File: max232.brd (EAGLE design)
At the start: 60 x 50 mm, 82 parts, among them U1 MAX3232CDE4, U2 MAX3232CDE4

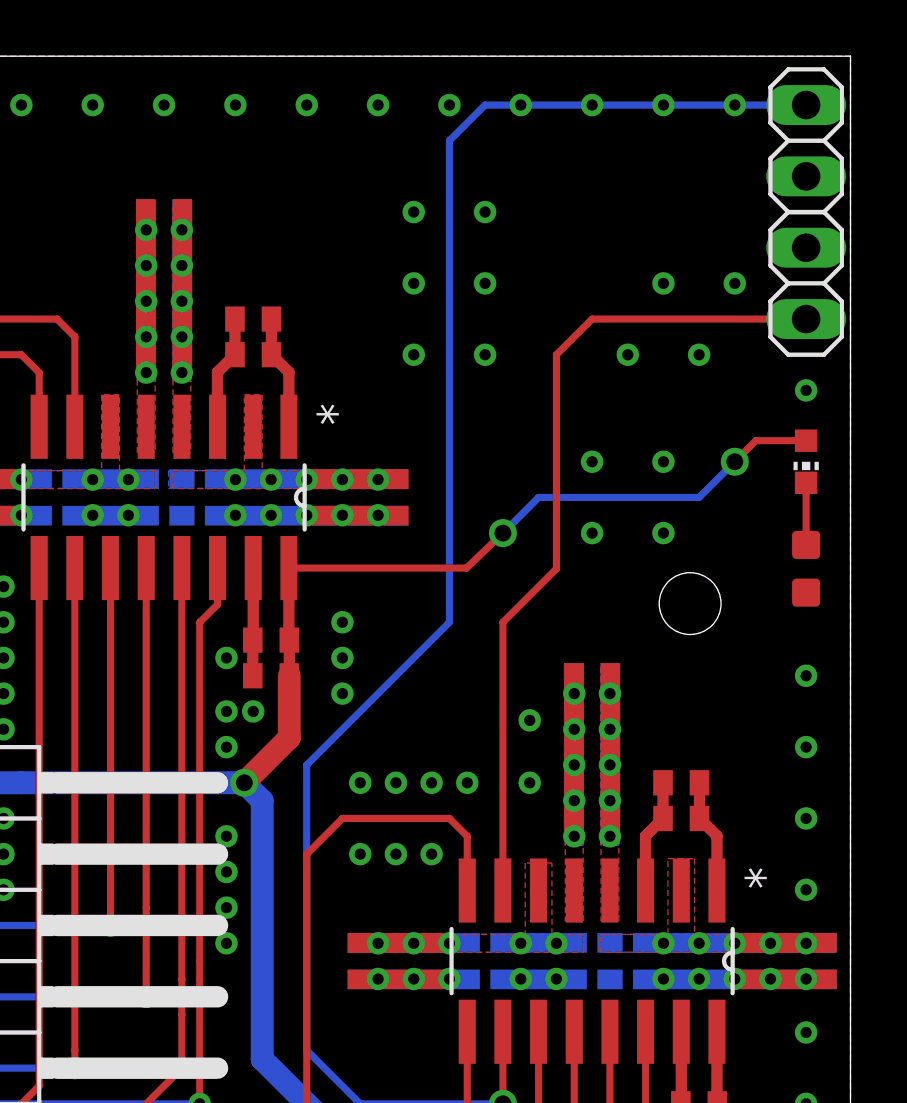
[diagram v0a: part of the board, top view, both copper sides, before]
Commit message: fixed DRC in max232
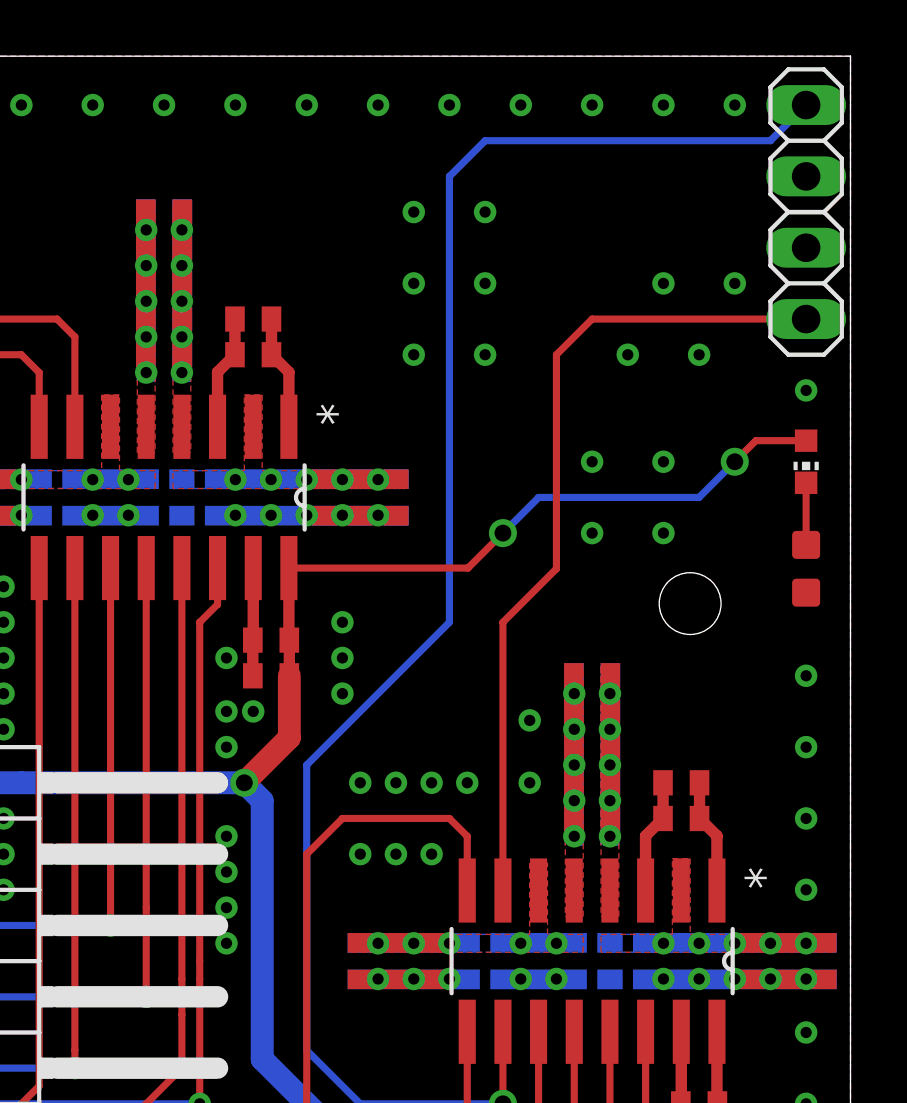
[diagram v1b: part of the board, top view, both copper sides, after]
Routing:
- net TIN: track 58.1 -> 57.3 mm
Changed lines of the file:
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@@
 <setting verticaltext="up"/>
 </settings>
-<grid distance="0.05" unitdist="inch" unit="mm" style="lines" multiple="1" display="no" altdistance="12.5" altunitdist="mil" altunit="mm"/>
+<grid distance="0.05" unitdist="inch" unit="mm" style="lines" multiple="1" display="no" altdistance="6.25" altunitdist="mil" altunit="mil"/>
 <layers>
 <layer number="1" name="Top" color="4" fill="1" visible="yes" active="yes"/>
@@
 <wire x1="55.245" y1="11.415" x2="55.26" y2="11.43" width="0.8128" layer="1"/>
 <wire x1="40.02" y1="25.7325" x2="38.4175" y2="24.13" width="0.8128" layer="1"/>
-<wire x1="40.005" y1="31.7754" x2="46.3296" y2="31.7754" width="0.254" layer="1"/>
-<wire x1="46.3296" y1="31.7754" x2="47.625" y2="33.02" width="0.254" layer="1"/>
 <via x="47.625" y="33.02" extent="1-16" drill="0.6"/>
 <wire x1="47.625" y1="33.02" x2="48.895" y2="34.29" width="0.254" layer="16"/>
@@
 <wire x1="56.63" y1="36.31" x2="58.42" y2="36.31" width="0.254" layer="1"/>
 <wire x1="27.94" y1="25.82" x2="27.94" y2="24.13" width="0.254" layer="16"/>
+<wire x1="40.005" y1="31.7754" x2="46.3804" y2="31.7754" width="0.254" layer="1"/>
+<wire x1="46.3804" y1="31.7754" x2="47.625" y2="33.02" width="0.254" layer="1"/>
 </signal>
 <signal name="GND">
@@
 <via x="40.64" y="34.925" extent="1-16" drill="0.4"/>
 <polygon width="0.4064" layer="16">
-<vertex x="35.71875" y="35.2425"/>
-<vertex x="35.71875" y="34.6075"/>
+<vertex x="35.8775" y="35.2425"/>
+<vertex x="35.8775" y="34.6075"/>
 <vertex x="44.1325" y="34.6075"/>
 <vertex x="44.1325" y="35.2425"/>
@@
 <vertex x="51.1175" y="18.0975"/>
 <vertex x="51.1175" y="18.7325"/>
-<vertex x="53.49875" y="18.7325"/>
-<vertex x="53.49875" y="21.43125"/>
-<vertex x="54.45125" y="21.43125"/>
-<vertex x="54.45125" y="18.7325"/>
+<vertex x="53.6575" y="18.7325"/>
+<vertex x="53.6575" y="21.43125"/>
+<vertex x="54.2925" y="21.43125"/>
+<vertex x="54.2925" y="18.7325"/>
 </polygon>
 <polygon width="0.4064" layer="16">
@@
 <vertex x="50.4825" y="18.0975"/>
 <vertex x="50.4825" y="18.7325"/>
-<vertex x="49.37125" y="18.7325"/>
-<vertex x="49.37125" y="21.2725"/>
-<vertex x="48.41875" y="21.2725"/>
-<vertex x="48.41875" y="18.7325"/>
+<vertex x="49.2125" y="18.7325"/>
+<vertex x="49.2125" y="21.2725"/>
+<vertex x="48.5775" y="21.2725"/>
+<vertex x="48.5775" y="18.7325"/>
 </polygon>
 <wire x1="43.18" y1="18.415" x2="42.56" y2="18.415" width="0.254" layer="1"/>
@@
 <polygon width="0.4064" layer="1">
 <vertex x="49.8475" y="28.2575"/>
-<vertex x="49.8475" y="19.20875"/>
-<vertex x="50.4825" y="19.20875"/>
+<vertex x="49.8475" y="19.3675"/>
+<vertex x="50.4825" y="19.3675"/>
 <vertex x="50.4825" y="28.2575"/>
 </polygon>
@@
 <polygon width="0.4064" layer="1">
 <vertex x="51.1175" y="28.2575"/>
-<vertex x="51.1175" y="19.20875"/>
-<vertex x="51.7525" y="19.20875"/>
+<vertex x="51.1175" y="19.3675"/>
+<vertex x="51.7525" y="19.3675"/>
 <vertex x="51.7525" y="28.2575"/>
 </polygon>
@@
 <wire x1="40.64" y1="14.605" x2="40.64" y2="24.765" width="0.254" layer="16"/>
 <wire x1="40.64" y1="24.765" x2="45.72" y2="29.845" width="0.254" layer="16"/>
-<wire x1="45.72" y1="29.845" x2="45.72" y2="46.99" width="0.254" layer="16"/>
-<wire x1="45.72" y1="46.99" x2="46.99" y2="48.26" width="0.254" layer="16"/>
-<wire x1="46.99" y1="48.26" x2="58.42" y2="48.26" width="0.254" layer="16"/>
+<wire x1="45.72" y1="29.845" x2="45.72" y2="45.72" width="0.254" layer="16"/>
+<wire x1="45.72" y1="45.72" x2="46.99" y2="46.99" width="0.254" layer="16"/>
+<wire x1="46.99" y1="46.99" x2="57.15" y2="46.99" width="0.254" layer="16"/>
+<wire x1="57.15" y1="46.99" x2="58.42" y2="48.26" width="0.254" layer="16"/>
 </signal>
 <signal name="ROUT">

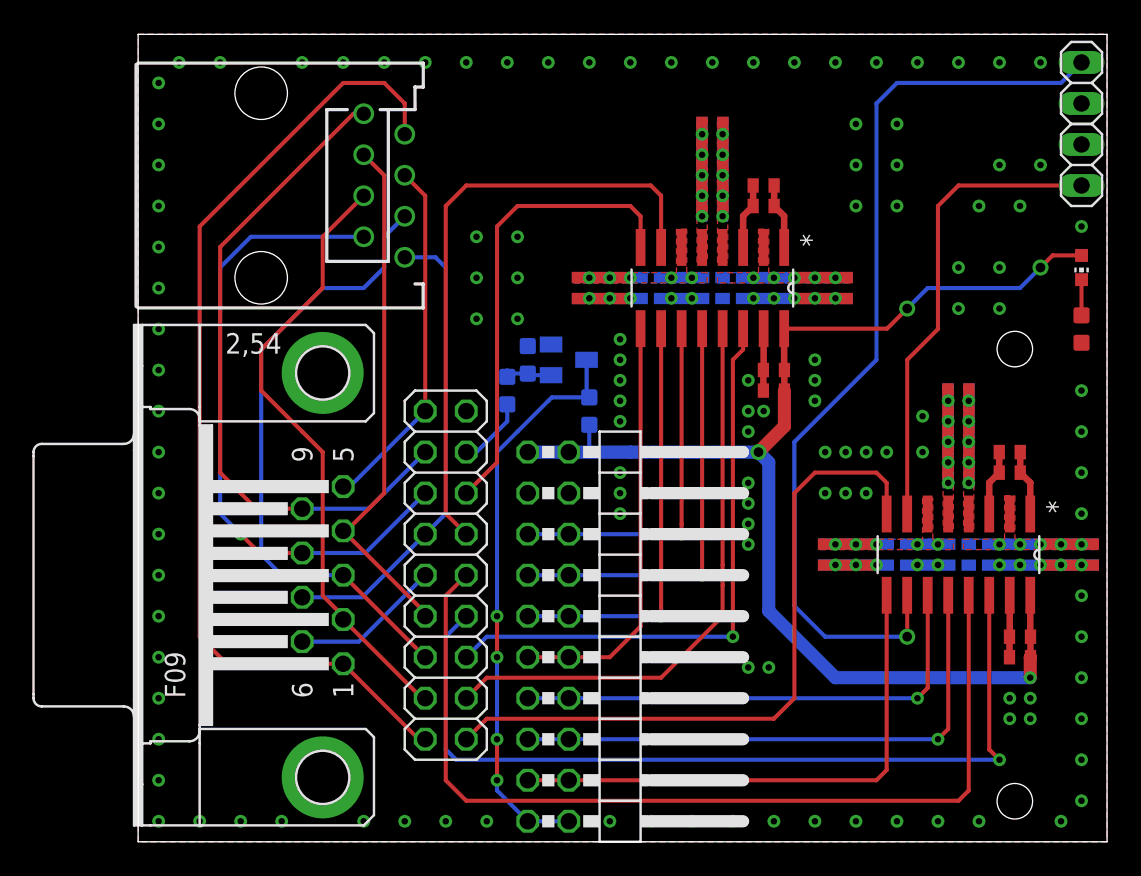
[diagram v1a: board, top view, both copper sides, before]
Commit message: updated libraries and fixed DRC
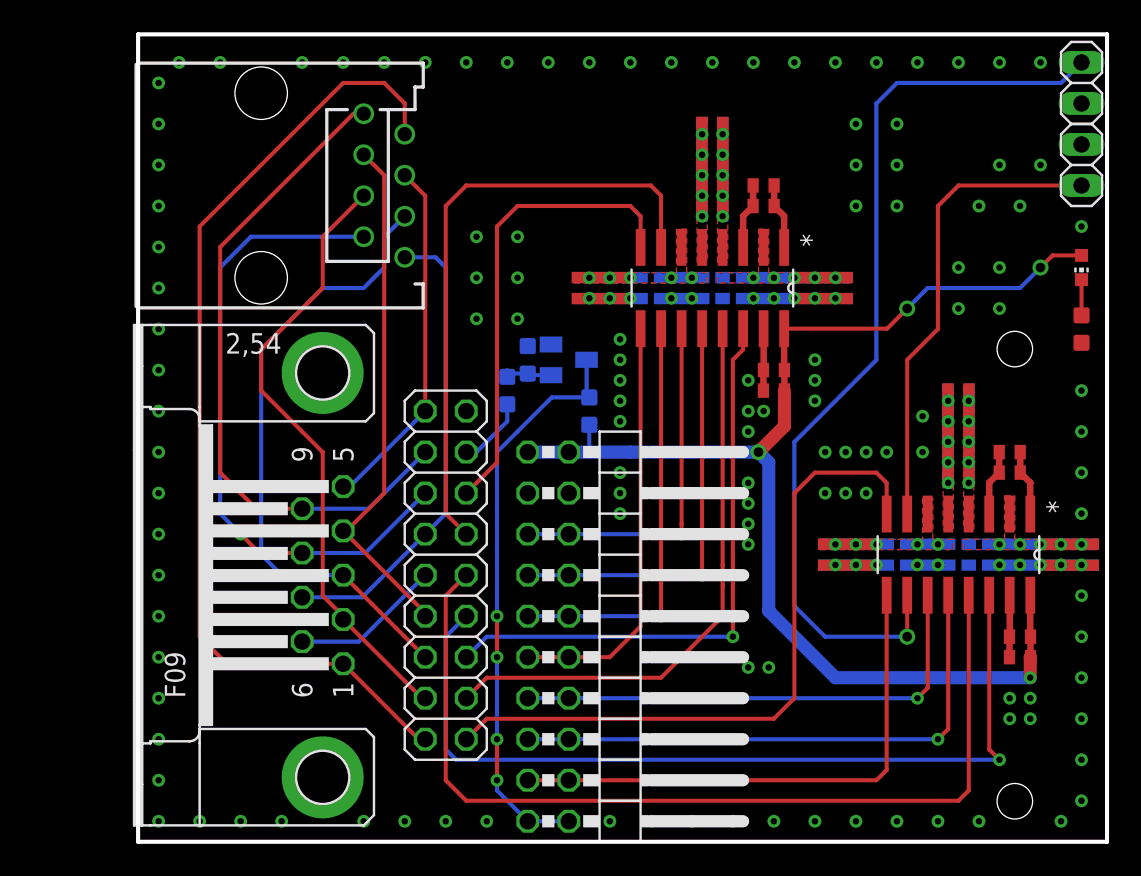
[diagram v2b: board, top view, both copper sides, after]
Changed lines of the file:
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@@
 <layer number="97" name="Info" color="7" fill="1" visible="no" active="no"/>
 <layer number="98" name="Guide" color="6" fill="1" visible="no" active="no"/>
+<layer number="100" name="tPlaceOutOfBoard" color="7" fill="1" visible="yes" active="yes"/>
+<layer number="101" name="bPlaceOutOfBoard" color="7" fill="1" visible="yes" active="yes"/>
 </layers>
 <board>
 <plain>
-<wire x1="0" y1="0" x2="60" y2="0" width="0" layer="20"/>
-<wire x1="60" y1="0" x2="60" y2="50" width="0" layer="20"/>
-<wire x1="60" y1="50" x2="0" y2="50" width="0" layer="20"/>
-<wire x1="0" y1="50" x2="0" y2="0" width="0" layer="20"/>
+<wire x1="0" y1="0" x2="60" y2="0" width="0.254" layer="20"/>
+<wire x1="60" y1="0" x2="60" y2="50" width="0.254" layer="20"/>
+<wire x1="60" y1="50" x2="0" y2="50" width="0.254" layer="20"/>
+<wire x1="0" y1="50" x2="0" y2="0" width="0.254" layer="20"/>
 <wire x1="41.29" y1="0.01" x2="41.29" y2="33.01" width="0" layer="47"/>
 <wire x1="41.29" y1="33.01" x2="67.29" y2="33.01" width="0" layer="47"/>
